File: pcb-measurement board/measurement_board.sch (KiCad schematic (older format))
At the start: 81 parts, among them P1 CONN_02X15, P2 CONN_02X13, Q2 Si1101X, U1 TPS73125, U10 AD8603, U13 TPS73133, U14 MCP4921, U15 74CBTLV3253, U5 MSP430G2955, U9 TLV1G125

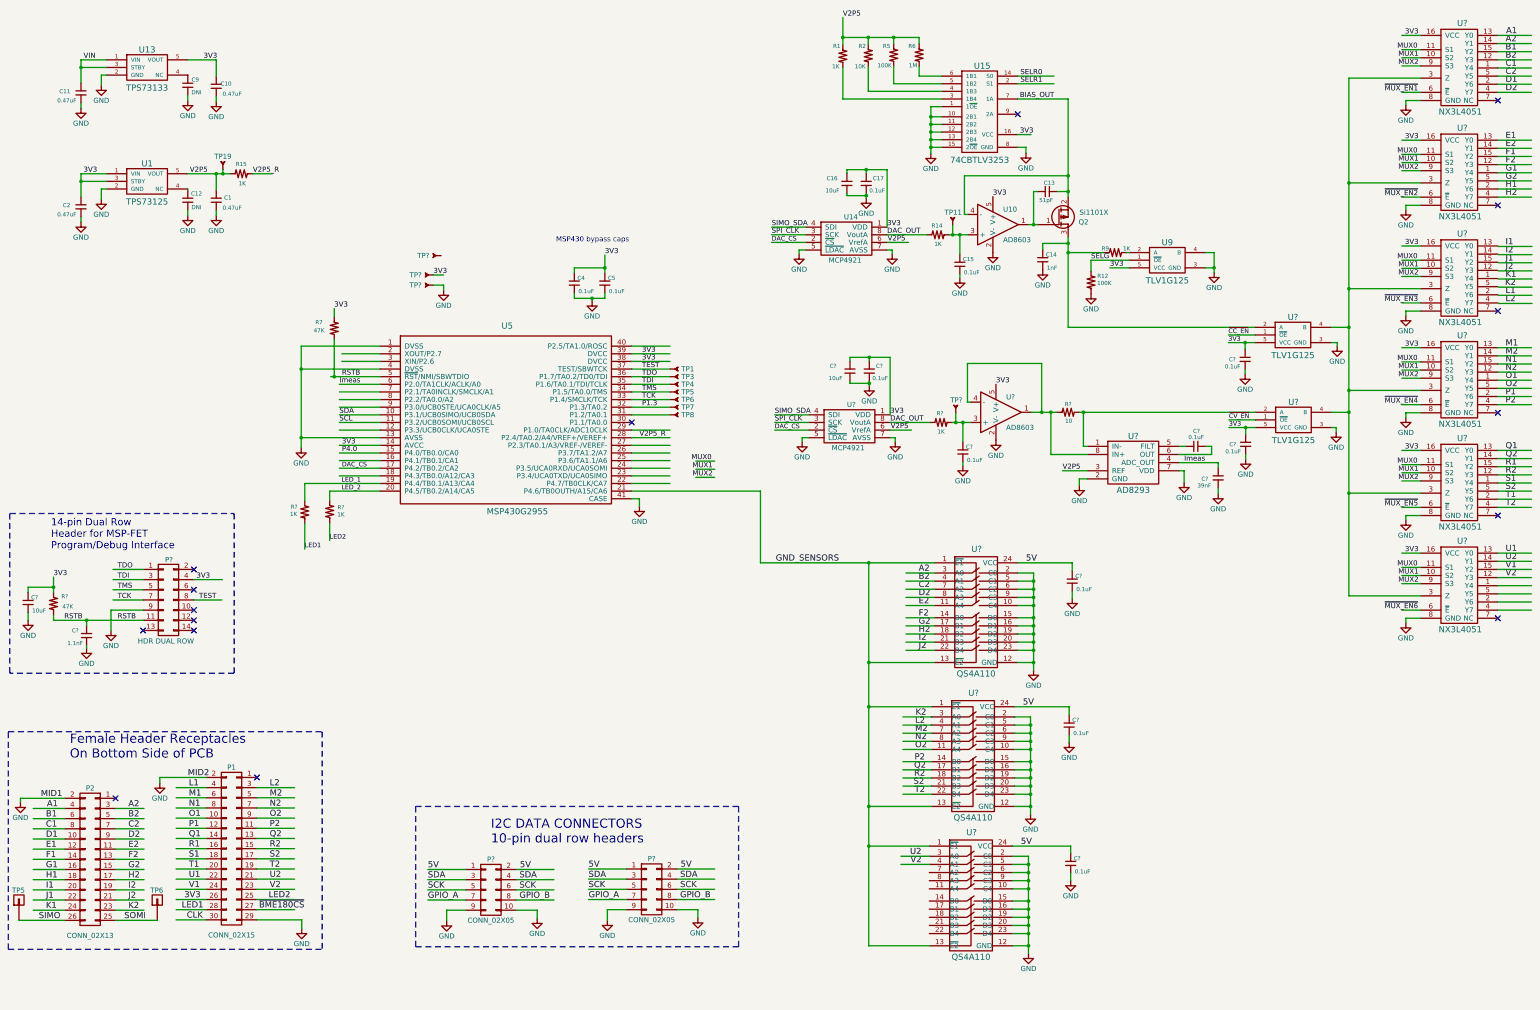
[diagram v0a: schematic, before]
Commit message: -schematic is being refined -working on placement of pcb parts -all footprints are completed
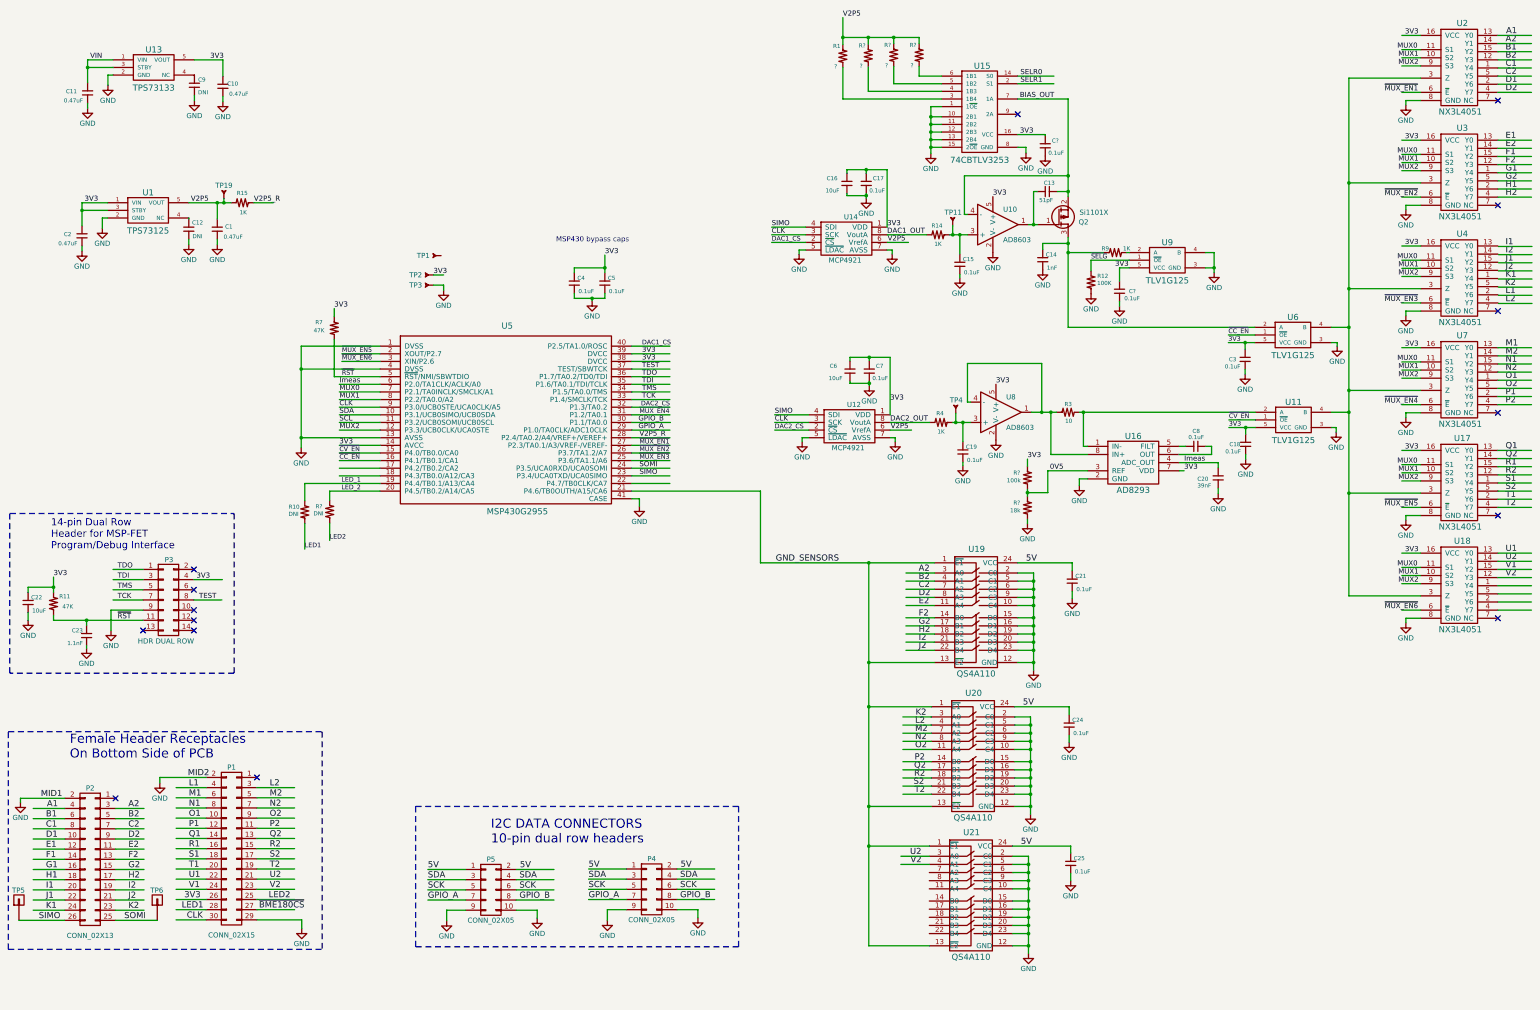
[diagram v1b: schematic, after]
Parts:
- removed R2: 10K, footprints_on_Cdrive:0402, symbol Res1_1
- removed R5: 100K, footprints_on_Cdrive:0402, symbol Res1_1
- removed R6: 1M, footprints_on_Cdrive:0402, symbol Res1_1
- removed R?: 1K, footprints_on_Cdrive:0402, symbol Res1_1
- removed TP1, TP3, TP4, TP5, TP6, TP7, TP8: TP_SMT_TnB, footprints_on_Cdrive:TP_SMT.02_top_bot, symbol TP_SMT_TnB
- added C? (x2): 0.1uF, footprints_on_Cdrive:0402, symbol CAP_NP
- added R?: 100k, footprints_on_Cdrive:0402, symbol Res1_1
- added R?: 18k, footprints_on_Cdrive:0402, symbol Res1_1
- added R?: DNI, footprints_on_Cdrive:0603, symbol Res1_1
- added R? (x3): ?, footprints_on_Cdrive:0603, symbol Res1_1
- P3: renamed from P?; footprint Pin_Headers:Pin_Header_Straight_2x07 -> Pin_Headers:Pin_Header_Straight_2x07_Pitch2.54mm
- R1: value 1K -> ?; footprint footprints_on_Cdrive:0402 -> footprints_on_Cdrive:0603; description RES SMD 1K OHM 1% 1/16W 0402 -> (none); manufacturer pn RC0402FR-071KL -> (none); supplier pn 311-1.00KLRCT-ND -> (none)
- R10: renamed from R?; value 1K -> DNI; footprint footprints_on_Cdrive:0402 -> footprints_on_Cdrive:0603; description RES SMD 1K OHM 1% 1/16W 0402 -> (none); manufacturer Yageo -> (none); manufacturer pn RC0402FR-071KL -> (none); supplier digikey -> (none); supplier pn 311-1.00KLRCT-ND -> (none)
- U15: manufacturer pn 74CBTLV3253BQ,115 -> 74CBTLV3253BQ-115
- U19, U20, U21: renamed from U?; description IC SWITCH 5PST, 24QSOP -> IC SWITCH 5PST 24QSOP; suppiler pn 800-1776-5-ND -> (none); supplier pn (none) -> 800-1776-5-ND
- gave numbers to parts that had none: 32
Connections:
- net labels added: 0V5, DAC1_CS, DAC1_OUT, DAC2_CS, DAC2_OUT, ~RST, ~SELG
- net labels removed: DAC_CS, DAC_OUT, P1.3, P4.0, RSTB, SELG, SIMO_SDA, SPI_CLK
- wire segments 476 -> 481
- no-connect marks 16 -> 15
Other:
- moved on the sheet: C1, C10, C11, C12, C2, C9, R15, TP19, U1, U13

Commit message: -component placement completed -routing just started
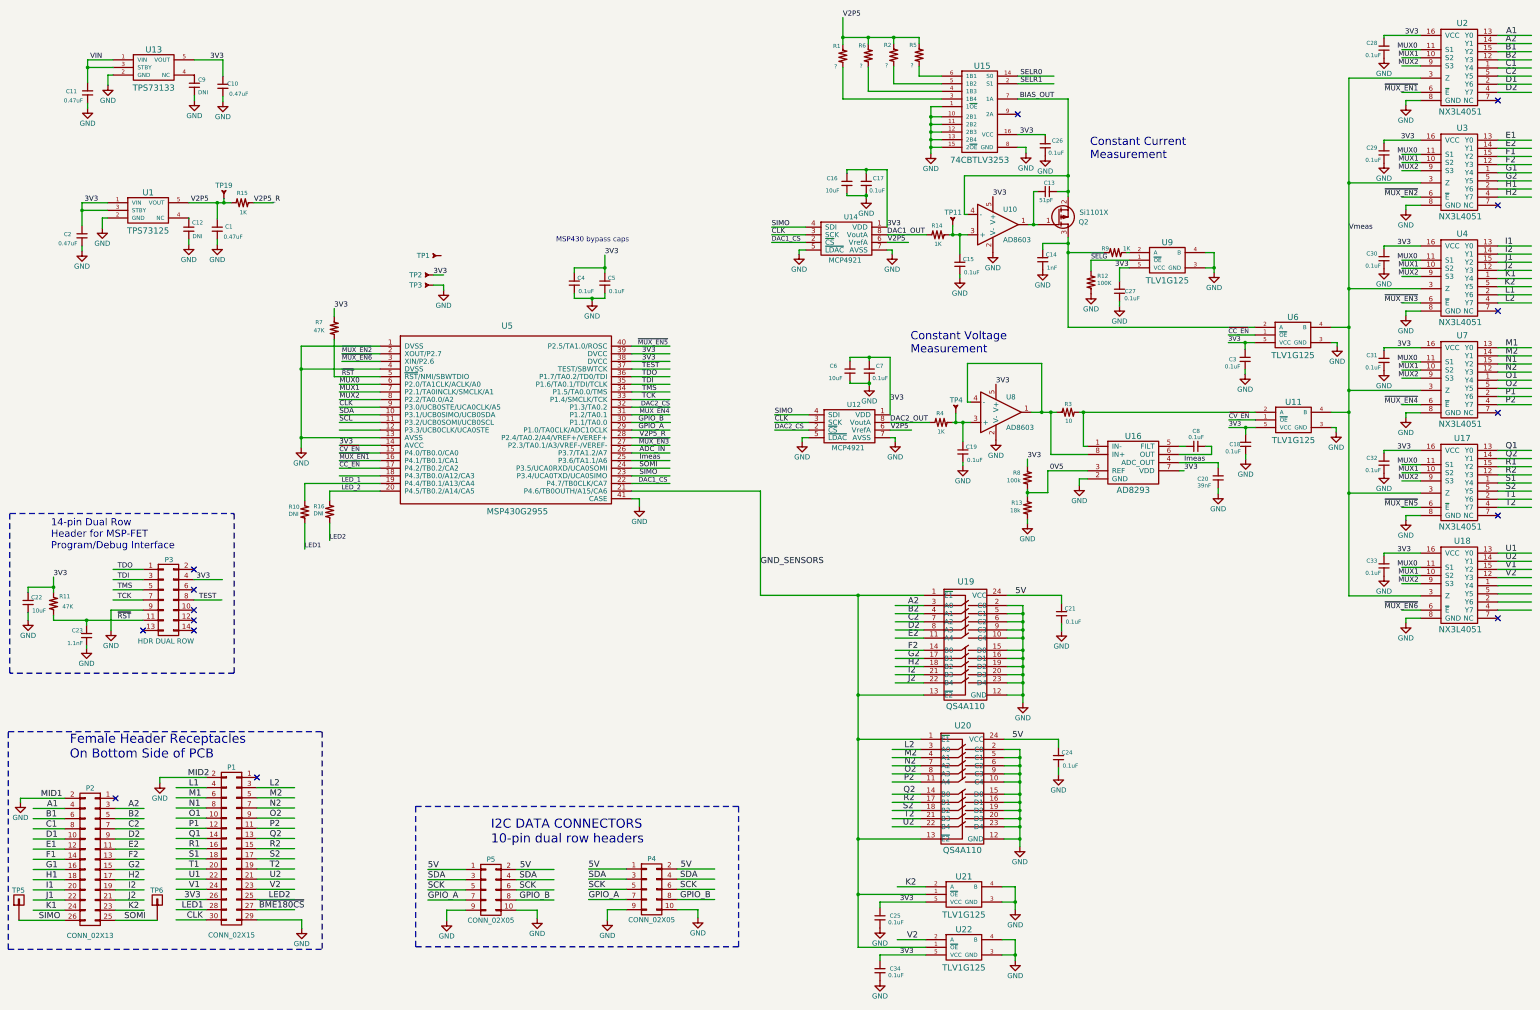
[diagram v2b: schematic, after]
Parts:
- removed U21: QS4A110, footprints_on_Cdrive:QSOP-24, symbol QS4A110
- added C28, C29, C30, C31, C32, C33, C34: 0.1uF, footprints_on_Cdrive:0402, symbol CAP_NP
- added U21, U22: TLV1G125, footprints_on_Cdrive:SOT23-5, symbol TLV1G125
- U16: footprint (none) -> footprints_on_Cdrive:SOT23-8
- gave numbers to parts that had none: 8
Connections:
- net labels added: ADC_IN, Vmeas
- wire segments 481 -> 482
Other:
- note added: "Constant Current\nMeasurement"
- note added: "Constant Voltage\nMeasurement"
- moved on the sheet: C21, C24, C25, U19, U20

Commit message: -replaced all measurement board 0402 components with 0603 -adjusted placement and started routing on the layout
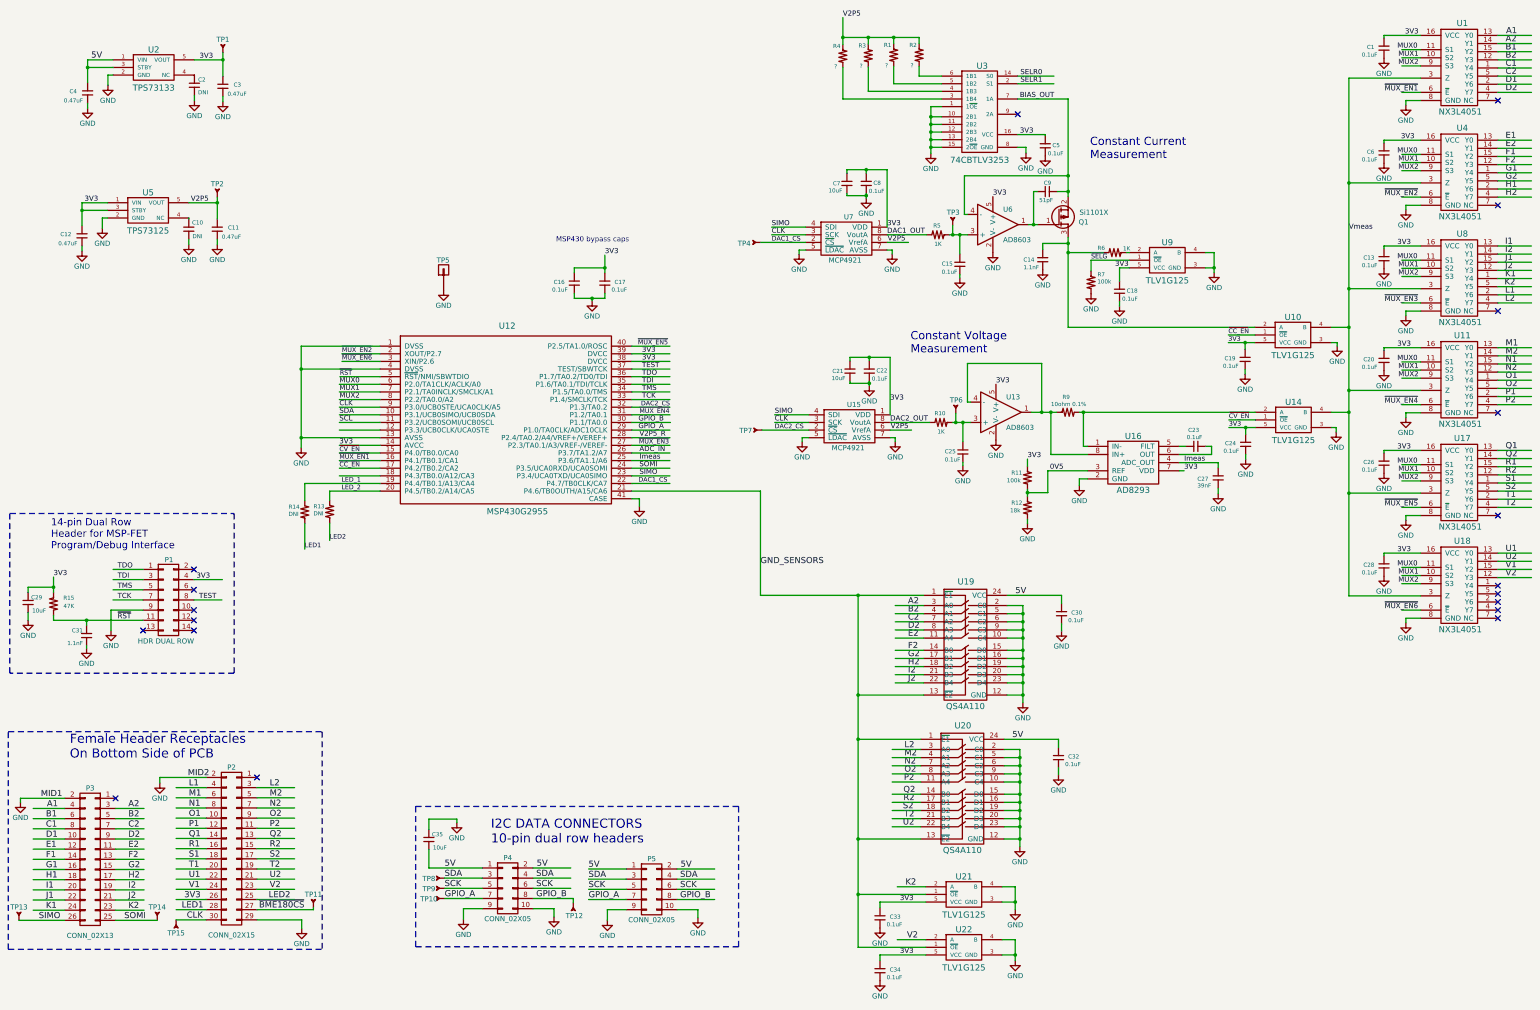
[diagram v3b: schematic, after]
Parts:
- removed C10, C2: 0.47uF, footprints_on_Cdrive:0402, symbol CAP_NP
- removed C27, C29, C31, C4: 0.1uF, footprints_on_Cdrive:0402, symbol CAP_NP
- removed R11: 47K, footprints_on_Cdrive:0402, symbol Res1
- removed R12: 100K, footprints_on_Cdrive:0402, symbol Res1_1
- removed R14, R9: 1K, footprints_on_Cdrive:0402, symbol Res1_1
- removed TP2, TP3: TP_SMT_TnB, footprints_on_Cdrive:TP_SMT.02_top_bot, symbol TP_SMT_TnB
- removed TP6: header_pin, footprints_on_Cdrive:Header_Pin_Rnd, symbol header_pin
- added C11, C12: 0.47uF, footprints_on_Cdrive:0603, symbol CAP_NP
- added C13, C20, C22, C23: 0.1uF, footprints_on_Cdrive:0603, symbol CAP_NP
- added C35: 10uF, footprints_on_Cdrive:0603, symbol CAP_NP
- added R5, R6: 1K, footprints_on_Cdrive:0603, symbol Res1_1
- added TP10, TP11, TP12, TP13, TP14, TP15, TP4, TP7, TP8, TP9: TP_SMT, footprints_on_Cdrive:TP_SMT.02, symbol TP_SMT
- C1: value 0.47uF -> 0.1uF; footprint footprints_on_Cdrive:0402 -> footprints_on_Cdrive:0603; description CAP CER 0.47UF 10V X5R 0402 -> CAP CER 0.1UF 16V X7R 0603; manufacturer Murata -> AVX Corporation; manufacturer pn GRM155R61A474KE15D -> GRM188R71C104KA01D; supplier pn 490-3264-1-ND -> 490-1532-1-ND
- C10: renamed from C12; footprint footprints_on_Cdrive:0402 -> footprints_on_Cdrive:0603
- C14: value 1nF -> 1.1nF; footprint footprints_on_Cdrive:0402 -> footprints_on_Cdrive:0603; description CAP CER 1000PF 50V X7R 0402 -> CAP CER 1100PF 50V C0G/NP0 0603; manufacturer pn GRM155R71H102KA01D -> GRM1885C1H112JA01D; supplier pn 490-1303-1-ND -> 490-1452-1-ND
- C15, C17, C18, C19, C24, C25, C26, C28, C5, C8: footprint footprints_on_Cdrive:0402 -> footprints_on_Cdrive:0603; description CAP CER 0.1UF 16V X5R 0402 -> CAP CER 0.1UF 16V X7R 0603; manufacturer pn 0402YD104KAT2A -> GRM188R71C104KA01D; supplier pn 478-1126-1-ND -> 490-1532-1-ND
- C16, C6: value 10uF -> 0.1uF; footprint footprints_on_Cdrive:0402 -> footprints_on_Cdrive:0603; description CAP CER 10UF 10V X5R 0402 -> CAP CER 0.1UF 16V X7R 0603; manufacturer Samsung -> AVX Corporation; manufacturer pn CL05A106MP8NUB8 -> GRM188R71C104KA01D; supplier pn 1276-6830-1-ND -> 490-1532-1-ND
- C2: renamed from C9; footprint footprints_on_Cdrive:0402 -> footprints_on_Cdrive:0603
- C21, C7: value 0.1uF -> 10uF; footprint footprints_on_Cdrive:0402 -> footprints_on_Cdrive:0603; description CAP CER 0.1UF 16V X5R 0402 -> CAP CER 10UF 6.3V X5R 0603; manufacturer AVX Corporation -> Murata; manufacturer pn 0402YD104KAT2A -> GRM188R60J106ME47D; supplier pn 478-1126-1-ND -> 490-3896-1-ND
- C27: renamed from C20; footprint footprints_on_Cdrive:0402 -> footprints_on_Cdrive:0603; description CAP CER 0.1UF 16V X5R 0402 -> CAP CER 0.039UF 16V X7R 0603; manufacturer AVX Corporation -> Kemet; manufacturer pn 0402YD104KAT2A -> C0603C393K4RACTU; supplier pn 478-1126-1-ND -> 399-9078-1-ND
- C29: renamed from C22; footprint footprints_on_Cdrive:0402 -> footprints_on_Cdrive:0603; description CAP CER 10UF 4V X5R 0402 -> CAP CER 10UF 6.3V X5R 0603; manufacturer pn GRM155R60G106ME44D -> GRM188R60J106ME47D; supplier pn 490-10693-1-ND -> 490-3896-1-ND
- C3: value 0.1uF -> 0.47uF; footprint footprints_on_Cdrive:0402 -> footprints_on_Cdrive:0603; description CAP CER 0.1UF 16V X5R 0402 -> CAP CER 0.47UF 10V X5R 0603; manufacturer AVX Corporation -> Samsung; manufacturer pn 0402YD104KAT2A -> CL10A474KP8NNNC; supplier pn 478-1126-1-ND -> 1276-1898-1-ND
- C30, C32, C33, C34: footprint footprints_on_Cdrive:0402 -> Resistors_SMD:R_0603_HandSoldering; description CAP CER 0.1UF 16V X5R 0402 -> CAP CER 0.1UF 16V X7R 0603; manufacturer pn 0402YD104KAT2A -> GRM188R71C104KA01D; supplier pn 478-1126-1-ND -> 490-1532-1-ND
- C31: renamed from C23; footprint footprints_on_Cdrive:0402 -> footprints_on_Cdrive:0603; description CAP CER 1100PF 50V NP0 0402 -> CAP CER 1100PF 50V C0G/NP0 0603; manufacturer Kemet -> Murata; manufacturer pn C0402C112J5GAC7867 -> GRM1885C1H112JA01D; supplier pn 399-9948-1-ND -> 490-1452-1-ND
- C4: renamed from C11; footprint footprints_on_Cdrive:0402 -> footprints_on_Cdrive:0603; description CAP CER 0.47UF 10V X5R 0402 -> CAP CER 0.47UF 10V X5R 0603; manufacturer Murata -> Samsung; manufacturer pn GRM155R61A474KE15D -> CL10A474KP8NNNC; supplier pn 490-3264-1-ND -> 1276-1898-1-ND
- C9: renamed from C13; footprint footprints_on_Cdrive:0402 -> footprints_on_Cdrive:0603; description CAP CER 51PF 50V NP0 0402 -> CAP CER 51PF 50V C0G/NP0 0603; manufacturer pn GRM1555C1H510JA01D -> GRM1885C1H510JA01D; supplier pn 490-5944-1-ND -> 490-1420-1-ND
- R10: renamed from R4; footprint footprints_on_Cdrive:0402 -> footprints_on_Cdrive:0603; description RES SMD 1K OHM 1% 1/16W 0402 -> RES SMD 1K OHM 1% 1/10W 0603; manufacturer pn RC0402FR-071KL -> RC0603FR-071KLL; supplier pn 311-1.00KLRCT-ND -> 311-1.00KHRCT-ND
- R11: renamed from R8; footprint footprints_on_Cdrive:0402 -> footprints_on_Cdrive:0603; description RES SMD 100K OHM 1% 1/16W 0402 -> RES SMD 100K OHM 1% 1/10W 0603; manufacturer Stackpole Electronics Inc. -> Yageo; manufacturer pn RC0402FR-07100KL -> RC0603FR-07100KL; supplier pn 311-100KLRCT-ND -> 311-100KHRCT-ND
- R12: renamed from R13; footprint footprints_on_Cdrive:0402 -> footprints_on_Cdrive:0603; description RES SMD 100K OHM 1% 1/16W 0402 -> RES SMD 18K OHM 1% 1/10W 0603; manufacturer Stackpole Electronics Inc. -> Yageo; manufacturer pn RC0402FR-07100KL -> RC0603FR-0718KL; supplier pn 311-100KLRCT-ND -> 311-18.0KHRCT-ND
- R15: value 1K -> 47K; footprint footprints_on_Cdrive:0402 -> footprints_on_Cdrive:0603; description RES SMD 1K OHM 1% 1/16W 0402 -> RES SMD 47K OHM 1% 1/10W 0603; manufacturer pn RC0402FR-071KL -> RC0603FR-0747KL; supplier pn 311-1.00KLRCT-ND -> 311-47.0KHRCT-ND
- R7: value 47K -> 100k; footprint footprints_on_Cdrive:0402 -> footprints_on_Cdrive:0603; description RES SMD 47K OHM 1% 1/16W 0402 -> RES SMD 100K OHM 1% 1/10W 0603; manufacturer Stackpole Electronics Inc. -> Yageo; manufacturer pn RMCF0402FT47K0 -> RC0603FR-07100KL; supplier pn RMCF0402FT47K0CT-ND -> 311-100KHRCT-ND
- R9: renamed from R3; value 10 -> 10ohm 0.1%; footprint footprints_on_Cdrive:0402 -> footprints_on_Cdrive:0805; description RES SMD 100K OHM 1% 1/16W 0402 -> RES SMD 10 OHM 0.1% 1/4W 0805; manufacturer Stackpole Electronics Inc. -> TE Connectivity; manufacturer pn RC0402FR-07100KL -> 2-1625868-7; supplier pn 311-100KLRCT-ND -> A110351CT-ND
- renumbered P3 to P1, P1 to P2, P2 to P3, P5 to P4, P4 to P5, Q2 to Q1, R2 to R1, R16 to R13, R10 to R14, R5 to R2, R6 to R3, R1 to R4, TP19 to TP2, TP11 to TP3, TP4 to TP6, U2 to U1, U6 to U10, U7 to U11, U5 to U12, U8 to U13, U11 to U14, U12 to U15, U13 to U2, U15 to U3, U3 to U4, U1 to U5, U10 to U6, U14 to U7, U4 to U8
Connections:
- net labels removed: VIN
- wire segments 482 -> 476
- no-connect marks 15 -> 19
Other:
- moved on the sheet: P4, TP2, TP5
